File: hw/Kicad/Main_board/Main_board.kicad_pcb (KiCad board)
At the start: 2 copper layers, 100 x 100 mm, 28 parts, among them J1 LIPO 2S, J10 DIST_FRONT, J11 SENSORES_LINEA, J12 DIST_DCHA, J2 MOT_IZQ, J3 TB6612FNG_A, J4 TB6612FNG_B, J5 DC-DC_5V, J6 HC-05, J7 MOT_DER, J8 DIST_IZQ, J9 CAMARA, SW1 SW_DPDT, SW2 SW_Push, SW3 SW_Push, U1 PCF8574

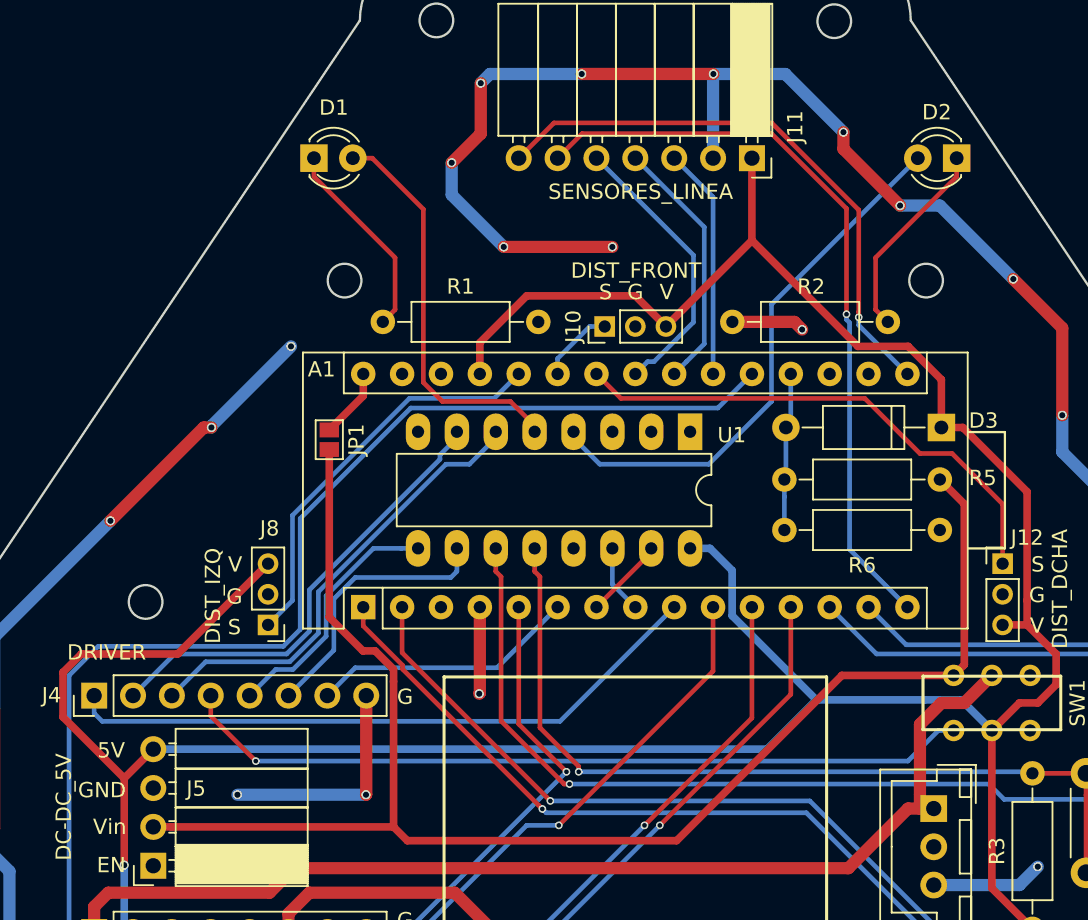
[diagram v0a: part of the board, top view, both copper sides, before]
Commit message: Leds connections modified and I2C resistors added
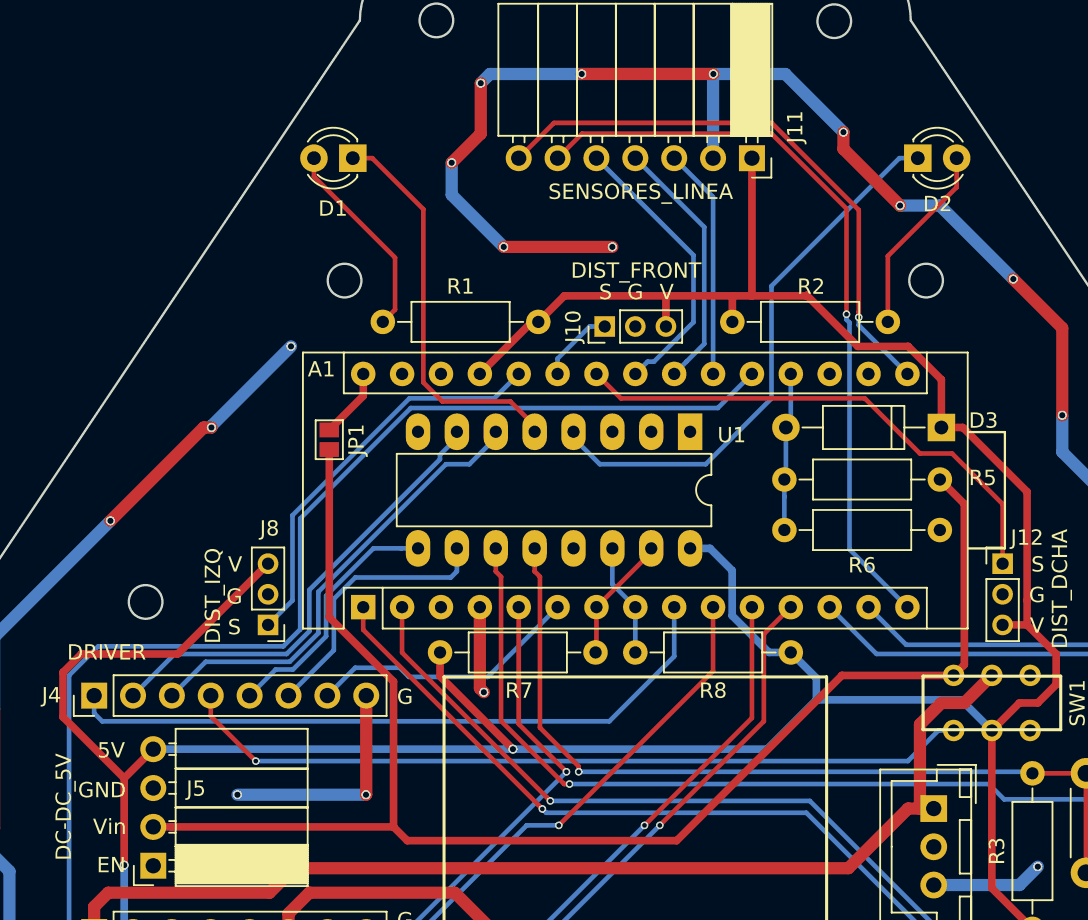
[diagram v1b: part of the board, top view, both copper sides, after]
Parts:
- added R7: 10K, Resistors_THT:R_Axial_DIN0207_L6.3mm_D2.5mm_P10.16mm_Horizontal, F.Cu at (147.4, 96.3)
- added R8: 10K, Resistors_THT:R_Axial_DIN0207_L6.3mm_D2.5mm_P10.16mm_Horizontal, F.Cu at (160.2, 96.3)
- moved D1 2.54 mm to (131.5, 64.0), turned to 180 degrees
- moved D2 2.54 mm to (168.5, 64.0), turned to 0 degrees
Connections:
- D1 pad 1: Net-(D1-Pad1) -> LED_R
- D1 pad 2: LED_R -> Net-(D1-Pad2)
- D2 pad 1: Net-(D2-Pad1) -> LED_G
- D2 pad 2: LED_G -> Net-(D2-Pad2)
- R1 pad 1: Net-(D1-Pad1) -> Net-(D1-Pad2)
- R1 pad 2: GND -> +5V
- R2 pad 1: Net-(D2-Pad1) -> Net-(D2-Pad2)
- R2 pad 2: GND -> +5V
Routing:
- net Net-(D2-Pad1): track 13.2 -> 0.00 mm
- net Net-(D1-Pad2): track 0.00 -> 13.2 mm
- net Net-(D1-Pad1): track 13.2 -> 0.00 mm
- net Net-(D2-Pad2): track 0.00 -> 12.6 mm
- net +5V: track 269.3 -> 280.0 mm, vias 1 -> 2
- net GND: track 327.5 -> 322.7 mm, vias 37 -> 36
- net I2C_SDA: track 5.32 -> 8.39 mm
- net I2C_SCL: track 4.46 -> 7.42 mm
- net PWM_IZQ: track 42.4 -> 44.3 mm
- net LED_G: track 36.0 -> 36.6 mm

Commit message: BOM modified
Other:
- board text added: "1. Black : - MOTOR 2. Red: + MOTOR 3. Brown: Hall SENSOR Vcc 4. Green: Hall SENSOR GND 5. Blue: Hall SENSOR B Vout 6. Purple: Hall SENSOR A Vout"
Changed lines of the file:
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@@
     (links 93)
     (no_connects 0)
-    (area 99.924999 49.924999 200.075001 150.075001)
+    (area 99.899999 44.8 200.100001 150.100001)
     (thickness 1.6)
-    (drawings 124)
+    (drawings 125)
     (tracks 434)
     (zones 0)
@@
     )
   )
+  (gr_text "1. Black : - MOTOR\n   2. Red: + MOTOR\n   3. Brown: Hall SENSOR Vcc\n   4. Green: Hall SENSOR GND\n   5. Blue: Hall SENSOR B Vout\n   6. Purple: Hall SENSOR A Vout" (at 119.7 156.8) (layer Eco2.User)
+    (effects (font (size 1.5 1.5) (thickness 0.3)))
+  )
   (gr_line (start 161 50) (end 163 50) (layer Edge.Cuts) (width 0.15))

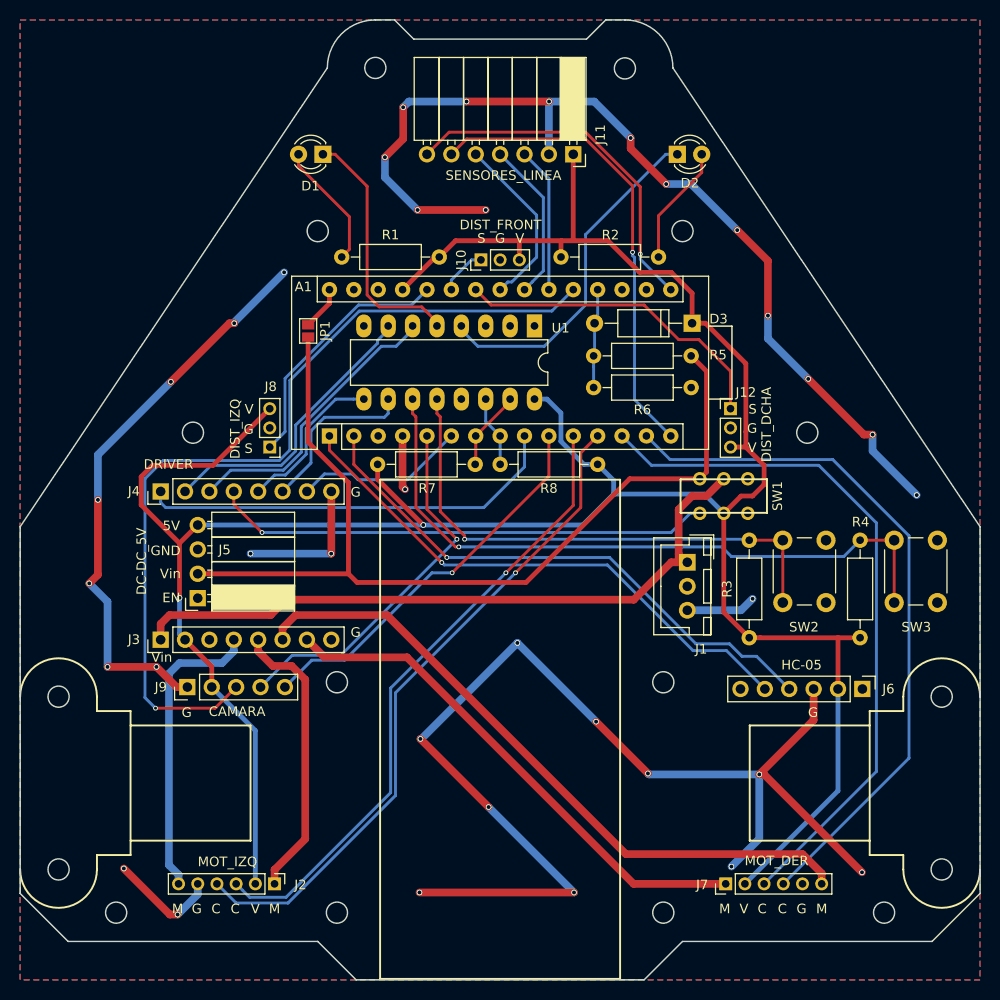
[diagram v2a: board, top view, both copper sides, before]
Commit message: Gerbers actualized and motors connector changed
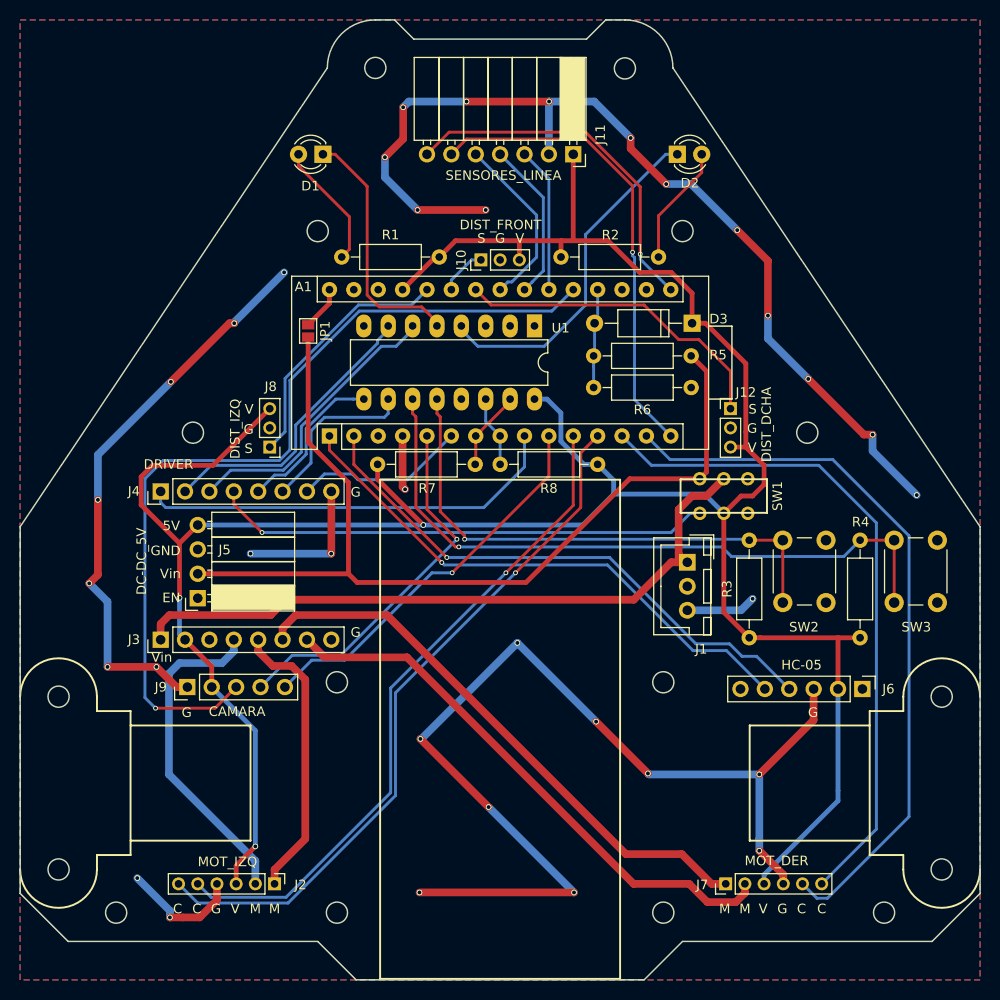
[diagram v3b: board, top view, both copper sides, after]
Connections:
- J2 pad 2: +5V -> M_IZQ_+
- J2 pad 3: ENC_IZQ_B -> +5V
- J2 pad 4: ENC_IZQ_A -> GND
- J2 pad 5: GND -> ENC_IZQ_B
- J2 pad 6: M_IZQ_+ -> ENC_IZQ_A
- J7 pad 1: M_DER_+ -> M_DER_-
- J7 pad 2: +5V -> M_DER_+
- J7 pad 3: ENC_DER_A -> +5V
- J7 pad 4: ENC_DER_B -> GND
- J7 pad 5: GND -> ENC_DER_B
- J7 pad 6: M_DER_- -> ENC_DER_A
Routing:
- net GND: track 322.7 -> 310.6 mm, vias 36 -> 35
- net M_DER_-: track 70.2 -> 59.5 mm
- net M_DER_+: track 54.2 -> 58.3 mm
- net ENC_IZQ_A: track 70.3 -> 74.3 mm
- net ENC_IZQ_B: track 66.2 -> 70.2 mm
- net M_IZQ_+: track 31.2 -> 34.6 mm
- net ENC_DER_B: track 73.3 -> 76.2 mm
- net ENC_DER_A: track 72.7 -> 70.2 mm
- net +5V: vias 2 -> 3
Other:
- board text added: "Cyclops-project"
- board text removed: "1. Black : - MOTOR 2. Red: + MOTOR 3. Brown: Hall SENSOR Vcc 4. Green: Hall SENSOR GND 5. Blue: Hall SENSOR B Vout 6. Purple: Hall SENSOR A Vout"

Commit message: PCB silk modified
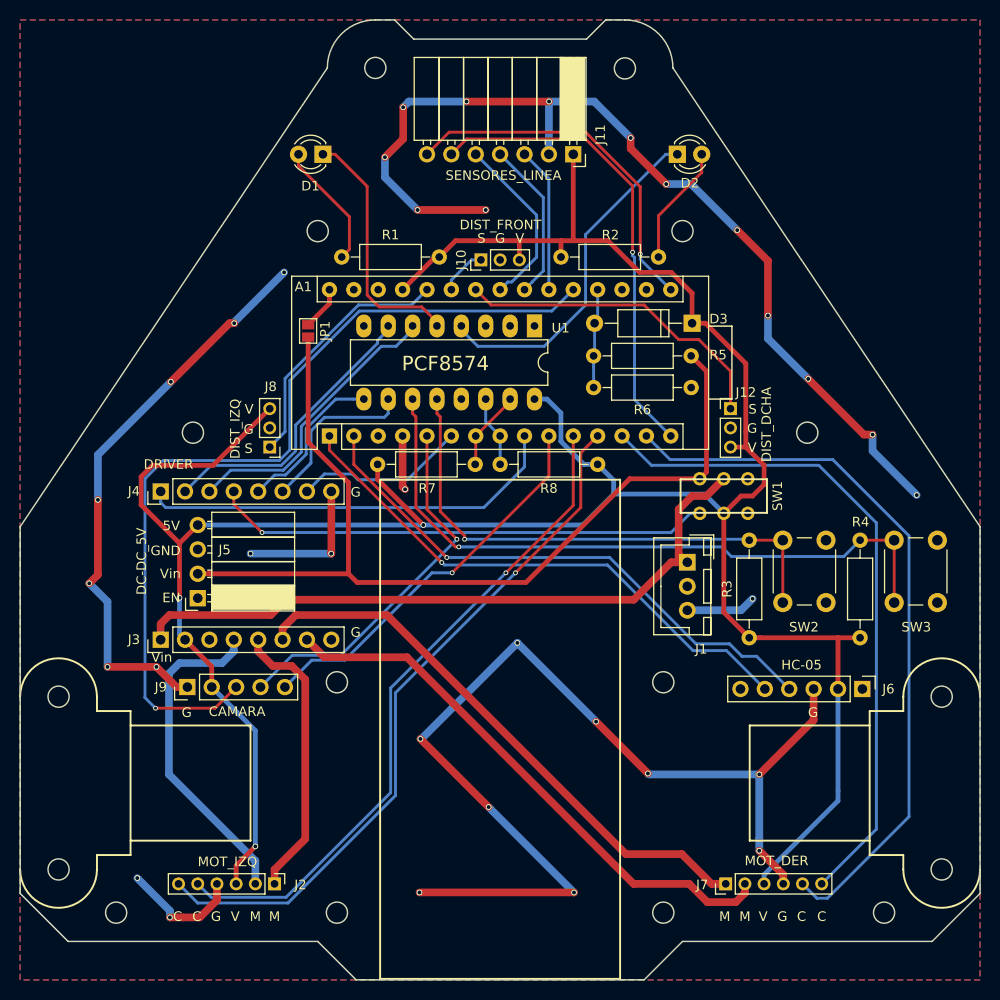
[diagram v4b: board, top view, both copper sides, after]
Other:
- board text added: "PCF8574"
- board text added: "github.com/Resaj/"
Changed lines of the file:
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@@
     (area 99.899999 44.8 200.100001 150.100001)
     (thickness 1.6)
-    (drawings 125)
+    (drawings 127)
     (tracks 445)
     (zones 0)
@@
     )
   )
+  (gr_text PCF8574 (at 144.3 85.8) (layer F.SilkS)
+    (effects (font (size 1.5 1.5) (thickness 0.2)))
+  )
+  (gr_text github.com/Resaj/ (at 151 99) (layer B.SilkS)
+    (effects (font (size 2.5 2.5) (thickness 0.4)) (justify mirror))
+  )
   (gr_text Cyclops-project (at 150 103.6) (layer B.SilkS)
     (effects (font (size 3 3) (thickness 0.5)) (justify mirror))
@@
     (effects (font (size 1 1) (thickness 0.2)))
   )
-  (gr_text G (at 179.4 142.6) (layer F.SilkS)
-    (effects (font (size 1 1) (thickness 0.2)))
-  )
-  (gr_text C (at 181.4 142.6) (layer F.SilkS)
-    (effects (font (size 1 1) (thickness 0.2)))
-  )
-  (gr_text C (at 183.5 142.6) (layer F.SilkS)
-    (effects (font (size 1 1) (thickness 0.2)))
-  )
-  (gr_text V (at 177.4 142.6) (layer F.SilkS)
-    (effects (font (size 1 1) (thickness 0.2)))
-  )
-  (gr_text M (at 175.5 142.6) (layer F.SilkS)
-    (effects (font (size 1 1) (thickness 0.2)))
-  )
-  (gr_text M (at 173.4 142.6) (layer F.SilkS)
-    (effects (font (size 1 1) (thickness 0.2)))
-  )
-  (gr_text C (at 118.4 142.6) (layer F.SilkS)
-    (effects (font (size 1 1) (thickness 0.2)))
-  )
-  (gr_text G (at 120.4 142.6) (layer F.SilkS)
-    (effects (font (size 1 1) (thickness 0.2)))
-  )
-  (gr_text C (at 116.4 142.6) (layer F.SilkS)
-    (effects (font (size 1 1) (thickness 0.2)))
-  )
-  (gr_text V (at 122.4 142.6) (layer F.SilkS)
-    (effects (font (size 1 1) (thickness 0.2)))
-  )
-  (gr_text M (at 126.5 142.6) (layer F.SilkS)
-    (effects (font (size 1 1) (thickness 0.2)))
-  )
-  (gr_text M (at 124.5 142.6) (layer F.SilkS)
-    (effects (font (size 1 1) (thickness 0.2)))
-  )
+  (gr_text G (at 179.4 143.4) (layer F.SilkS)
+    (effects (font (size 1 1) (thickness 0.2)))
+  )
+  (gr_text C (at 181.4 143.4) (layer F.SilkS)
+    (effects (font (size 1 1) (thickness 0.2)))
+  )
+  (gr_text C (at 183.5 143.4) (layer F.SilkS)
+    (effects (font (size 1 1) (thickness 0.2)))
+  )
+  (gr_text V (at 177.4 143.4) (layer F.SilkS)
+    (effects (font (size 1 1) (thickness 0.2)))
+  )
+  (gr_text M (at 175.5 143.4) (layer F.SilkS)
+    (effects (font (size 1 1) (thickness 0.2)))
+  )
+  (gr_text M (at 173.4 143.4) (layer F.SilkS)
+    (effects (font (size 1 1) (thickness 0.2)))
+  )
+  (gr_text C (at 118.4 143.4) (layer F.SilkS)
+    (effects (font (size 1 1) (thickness 0.2)))
+  )
+  (gr_text G (at 120.4 143.4) (layer F.SilkS)
+    (effects (font (size 1 1) (thickness 0.2)))
+  )
+  (gr_text C (at 116.4 143.4) (layer F.SilkS)
+    (effects (font (size 1 1) (thickness 0.2)))
+  )
+  (gr_text V (at 122.4 143.4) (layer F.SilkS)
+    (effects (font (size 1 1) (thickness 0.2)))
+  )
+  (gr_text M (at 126.5 143.4) (layer F.SilkS)
+    (effects (font (size 1 1) (thickness 0.2)))
+  )
+  (gr_text M (at 124.5 143.4) (layer F.SilkS)
+    (effects (font (size 1 1) (thickness 0.2)))
+  )

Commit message: PCBs silkscreen updated
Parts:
- removed the G*** at (150.0, 127.0)
- added G***: LOGO, Main_board:Logo Puma Pride, B.Cu at (150.0, 123.0)
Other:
- board text added: "Puma Pride Robotics Team"
- board text removed: "RESAJ"
- board text removed: "www.lnrc.es"
